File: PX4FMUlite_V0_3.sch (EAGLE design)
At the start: 143 parts, among them J2 DF13-4P-1.25V, J201 DF13C-6P-1.25V, J202 DF13C-6P-1.25V, J203 DF13C-6P-1.25V, J3 DF13C-4P-1.25V, J302 DF13C-4P-1.25V, J401 DF13C-4P-1.25V, J403 DF13C-7P-1.25V, J405 DF13C-4P-1.25V, J802 DF13C-3P-1.25V, M3_MOUNT1101 MOUNT-HOLE3.1MM, M3_MOUNT1102 MOUNT-HOLE3.1MM, M3_MOUNT1103 MOUNT-HOLE3.1MM, M3_MOUNT1104 MOUNT-HOLE3.1MM, U101 STM32F4X7VX, U2 MAX3051, U401 MAX3051, X101 3.2x2.5 mm / 24 MHz / 15 ppm

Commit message: More power routing
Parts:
- removed R101: 470R, pixhawk2:RESISTOR0402-RES
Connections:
- removed net IO-USART1_RX: L3G$4.P$1
- removed net IO-USART1_TX: R101.2
- removed net N$23: R101.1, U101PORTA_H.PA10
- new net SPEKTRUM_RX: L3G$4.P$1, U101PORTA_H.PA10
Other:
- note removed: "IO debug console"
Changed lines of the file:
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@@
 </part>
 <part name="GND39" library="pixhawk2" deviceset="GND" device=""/>
-<part name="R101" library="pixhawk2" deviceset="RESISTOR" device="0402-RES" value="470R">
-<attribute name="PARTNO" value="RC0402FR-07470RL"/>
-</part>
 <part name="R607" library="pixhawk2" deviceset="RESISTOR" device="0402-RES" value="10K">
 <attribute name="PARTNO" value="RC0402FR-0710KL"/>
@@
 </text>
 <text x="129.286" y="62.992" size="1.27" layer="91">Spare PWM output</text>
-<text x="68.58" y="134.62" size="1.27" layer="91">IO debug console</text>
 <text x="112.014" y="164.592" size="1.27" layer="91">Spare ADC</text>
 <text x="112.014" y="159.512" size="1.27" layer="91">Spare ADC</text>
@@
 <instance part="U101" gate="PORTE_H" x="165.1" y="129.54" rot="MR0"/>
 <instance part="U101" gate="OSC" x="165.1" y="91.44"/>
-<instance part="R101" gate="G$1" x="60.96" y="132.08">
-<attribute name="PARTNO" x="60.96" y="132.08" size="1.778" layer="96" display="off"/>
-</instance>
 </instances>
 <busses>
@@
 </segment>
 </net>
-<net name="N$23" class="0">
-<segment>
+<net name="SPEKTRUM_RX" class="0">
+<segment>
+<label x="63.5" y="132.08" size="1.27" layer="95" xref="yes"/>
 <pinref part="U101" gate="PORTA_H" pin="PA10"/>
-<pinref part="R101" gate="G$1" pin="1"/>
-<wire x1="33.02" y1="132.08" x2="55.88" y2="132.08" width="0.1524" layer="91"/>
-</segment>
-</net>
-<net name="IO-USART1_TX" class="0">
-<segment>
-<pinref part="R101" gate="G$1" pin="2"/>
-<wire x1="66.04" y1="132.08" x2="68.58" y2="132.08" width="0.1524" layer="91"/>
-<label x="68.58" y="132.08" size="1.27" layer="95" xref="yes"/>
+<wire x1="63.5" y1="132.08" x2="33.02" y2="132.08" width="0.1524" layer="91"/>
 </segment>
 </net>
@@
 <segment>
 <pinref part="U101" gate="PORTB_L" pin="PB5"/>
-<wire x1="33.02" y1="96.52" x2="48.26" y2="96.52" width="0.1524" layer="91"/>
-<label x="48.26" y="96.52" size="1.27" layer="95" xref="yes"/>
+<wire x1="33.02" y1="96.52" x2="53.34" y2="96.52" width="0.1524" layer="91"/>
+<label x="53.34" y="96.52" size="1.27" layer="95" xref="yes"/>
 </segment>
 </net>
@@
 <segment>
 <pinref part="U101" gate="PORTB_L" pin="PB7"/>
-<wire x1="33.02" y1="91.44" x2="38.1" y2="91.44" width="0.1524" layer="91"/>
-<label x="38.1" y="91.44" size="1.27" layer="95" xref="yes"/>
+<wire x1="33.02" y1="91.44" x2="58.42" y2="91.44" width="0.1524" layer="91"/>
+<label x="58.42" y="91.44" size="1.27" layer="95" xref="yes"/>
 </segment>
 </net>
@@
 </segment>
 </net>
-<net name="IO-USART1_RX" class="0">
+<net name="SPEKTRUM_RX" class="0">
 <segment>
 <label x="73.66" y="86.36" size="1.27" layer="95" font="vector" rot="R180" xref="yes"/>

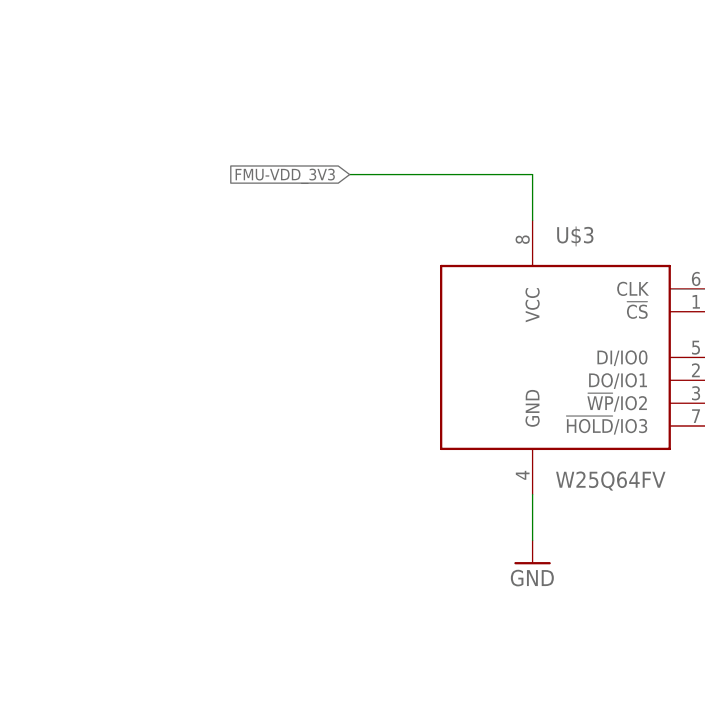
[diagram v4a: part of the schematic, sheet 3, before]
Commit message: Flash power decoupling
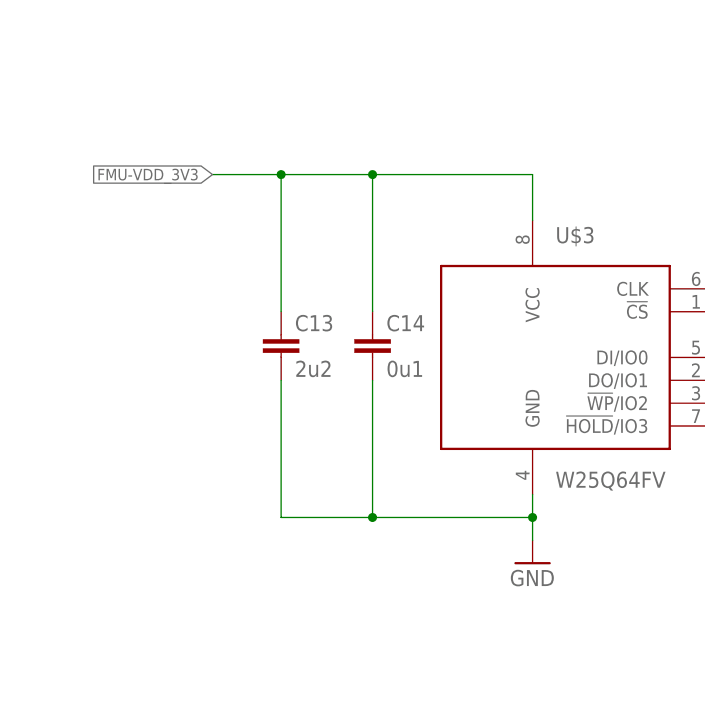
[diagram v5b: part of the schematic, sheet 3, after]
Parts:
- added C13: 2u2, pixhawk2:CAP0603
- added C14: 0u1, pixhawk2:CAP0402
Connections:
- net FMU-VDD_3V3: now also C13.1, C14.1
- net GND: now also C13.2, C14.2
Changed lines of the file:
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@@
 </part>
 <part name="U$14" library="PX4lite" deviceset="HEADER-3X1" device="RA"/>
+<part name="C13" library="pixhawk2" deviceset="CAP" device="0603" value="2u2">
+<attribute name="PARTNO" value="C1608Y5V1C225Z"/>
+</part>
+<part name="C14" library="pixhawk2" deviceset="CAP" device="0402" value="0u1">
+<attribute name="PARTNO" value="CC0402ZRY5V7BB104"/>
+</part>
 </parts>
 <sheets>
@@
 <instance part="GND12" gate="1" x="76.2" y="27.94"/>
 <instance part="U$5" gate="G$1" x="53.34" y="134.62"/>
+<instance part="C13" gate="G$1" x="48.26" y="50.8">
+<attribute name="PARTNO" x="48.26" y="50.8" size="1.778" layer="96" display="off"/>
+</instance>
+<instance part="C14" gate="G$1" x="58.42" y="50.8">
+<attribute name="PARTNO" x="58.42" y="50.8" size="1.778" layer="96" display="off"/>
+</instance>
 </instances>
 <busses>
@@
 </segment>
 <segment>
-<label x="55.88" y="71.12" size="1.27" layer="95" rot="R180" xref="yes"/>
-<wire x1="76.2" y1="71.12" x2="55.88" y2="71.12" width="0.1524" layer="91"/>
+<label x="40.64" y="71.12" size="1.27" layer="95" rot="R180" xref="yes"/>
+<wire x1="76.2" y1="71.12" x2="58.42" y2="71.12" width="0.1524" layer="91"/>
 <pinref part="U$3" gate="G$1" pin="VCC"/>
+<wire x1="58.42" y1="71.12" x2="48.26" y2="71.12" width="0.1524" layer="91"/>
+<wire x1="48.26" y1="71.12" x2="40.64" y2="71.12" width="0.1524" layer="91"/>
 <wire x1="76.2" y1="71.12" x2="76.2" y2="66.04" width="0.1524" layer="91"/>
+<pinref part="C13" gate="G$1" pin="1"/>
+<wire x1="48.26" y1="55.88" x2="48.26" y2="71.12" width="0.1524" layer="91"/>
+<pinref part="C14" gate="G$1" pin="1"/>
+<wire x1="58.42" y1="55.88" x2="58.42" y2="71.12" width="0.1524" layer="91"/>
+<junction x="58.42" y="71.12"/>
+<junction x="48.26" y="71.12"/>
 </segment>
 </net>
@@
 <pinref part="U$3" gate="G$1" pin="GND"/>
 <pinref part="GND12" gate="1" pin="GND"/>
-<wire x1="76.2" y1="35.56" x2="76.2" y2="30.48" width="0.1524" layer="91"/>
-</segment>
-<segment>
+<wire x1="76.2" y1="35.56" x2="76.2" y2="33.02" width="0.1524" layer="91"/>
+<pinref part="C13" gate="G$1" pin="2"/>
+<wire x1="76.2" y1="33.02" x2="76.2" y2="30.48" width="0.1524" layer="91"/>
+<wire x1="76.2" y1="33.02" x2="58.42" y2="33.02" width="0.1524" layer="91"/>
+<wire x1="58.42" y1="33.02" x2="48.26" y2="33.02" width="0.1524" layer="91"/>
+<wire x1="48.26" y1="33.02" x2="48.26" y2="48.26" width="0.1524" layer="91"/>
+<pinref part="C14" gate="G$1" pin="2"/>
+<wire x1="58.42" y1="48.26" x2="58.42" y2="33.02" width="0.1524" layer="91"/>
+<junction x="58.42" y="33.02"/>
+<junction x="76.2" y="33.02"/>
+</segment>
+<segment>

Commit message: More stuff
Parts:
- added C15: 0u1, pixhawk2:CAP0402
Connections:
- net FMU-VDD_3V3: now also C15.1
- net GND: now also C15.2
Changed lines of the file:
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@@
+<attribute name="PARTNO" value="CC0402ZRY5V7BB104"/>
+</part>
+<part name="C15" library="pixhawk2" deviceset="CAP" device="0402" value="0u1">
 <attribute name="PARTNO" value="CC0402ZRY5V7BB104"/>
 </part>
@@
 <attribute name="PARTNO" x="40.64" y="132.08" size="1.778" layer="96" display="off"/>
 </instance>
+<instance part="C15" gate="G$1" x="170.18" y="157.48">
+<attribute name="PARTNO" x="170.18" y="157.48" size="1.778" layer="96" display="off"/>
+</instance>
 </instances>
 <busses>
@@
 <junction x="220.98" y="139.7"/>
 <junction x="228.6" y="139.7"/>
+<pinref part="C15" gate="G$1" pin="2"/>
+<wire x1="170.18" y1="154.94" x2="170.18" y2="139.7" width="0.1524" layer="91"/>
+<wire x1="170.18" y1="139.7" x2="180.34" y2="139.7" width="0.1524" layer="91"/>
+<junction x="180.34" y="139.7"/>
 </segment>
 <segment>
@@
 <junction x="200.66" y="165.1"/>
 <junction x="190.5" y="165.1"/>
-<wire x1="180.34" y1="165.1" x2="177.8" y2="165.1" width="0.1524" layer="91"/>
-<label x="177.8" y="165.1" size="1.27" layer="95" rot="R180" xref="yes"/>
+<wire x1="180.34" y1="165.1" x2="170.18" y2="165.1" width="0.1524" layer="91"/>
+<label x="167.64" y="165.1" size="1.27" layer="95" rot="R180" xref="yes"/>
 <junction x="180.34" y="165.1"/>
-</segment>
-<segment>
+<pinref part="C15" gate="G$1" pin="1"/>
+<wire x1="170.18" y1="165.1" x2="167.64" y2="165.1" width="0.1524" layer="91"/>
+<wire x1="170.18" y1="162.56" x2="170.18" y2="165.1" width="0.1524" layer="91"/>
+<junction x="170.18" y="165.1"/>
+</segment>
+<segment>
